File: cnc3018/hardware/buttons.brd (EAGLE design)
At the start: 56 x 20 mm, 4 parts

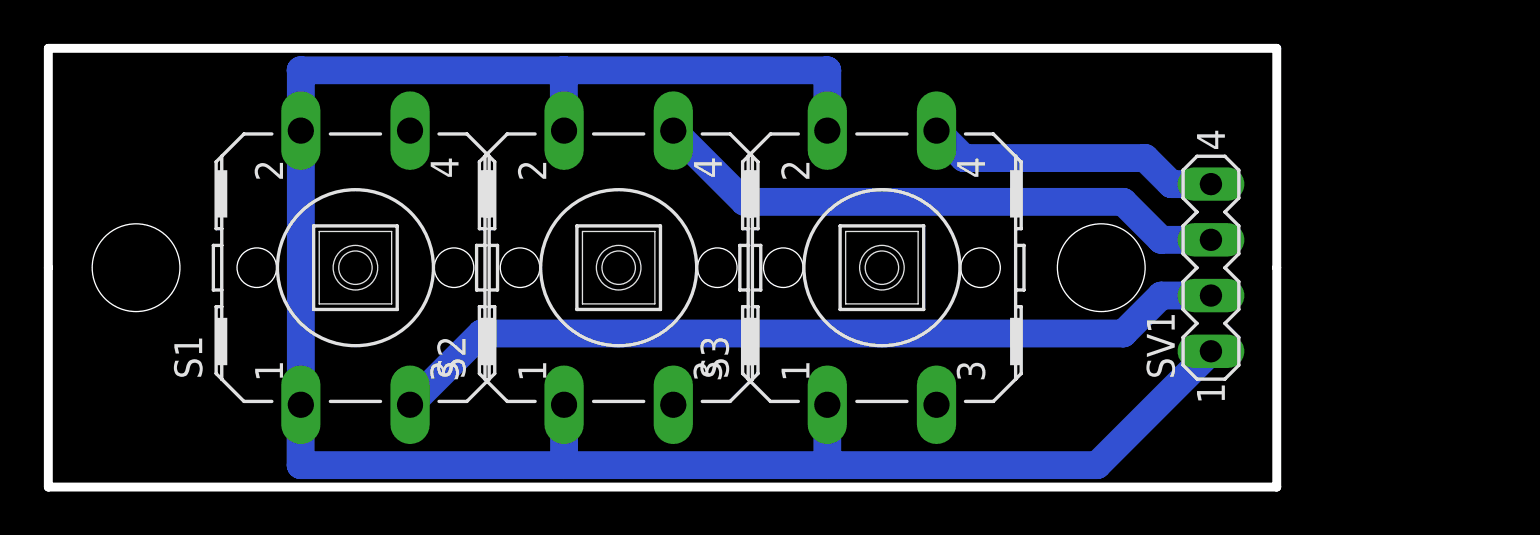
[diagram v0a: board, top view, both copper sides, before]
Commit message: cnc3018: changed buttons board + case
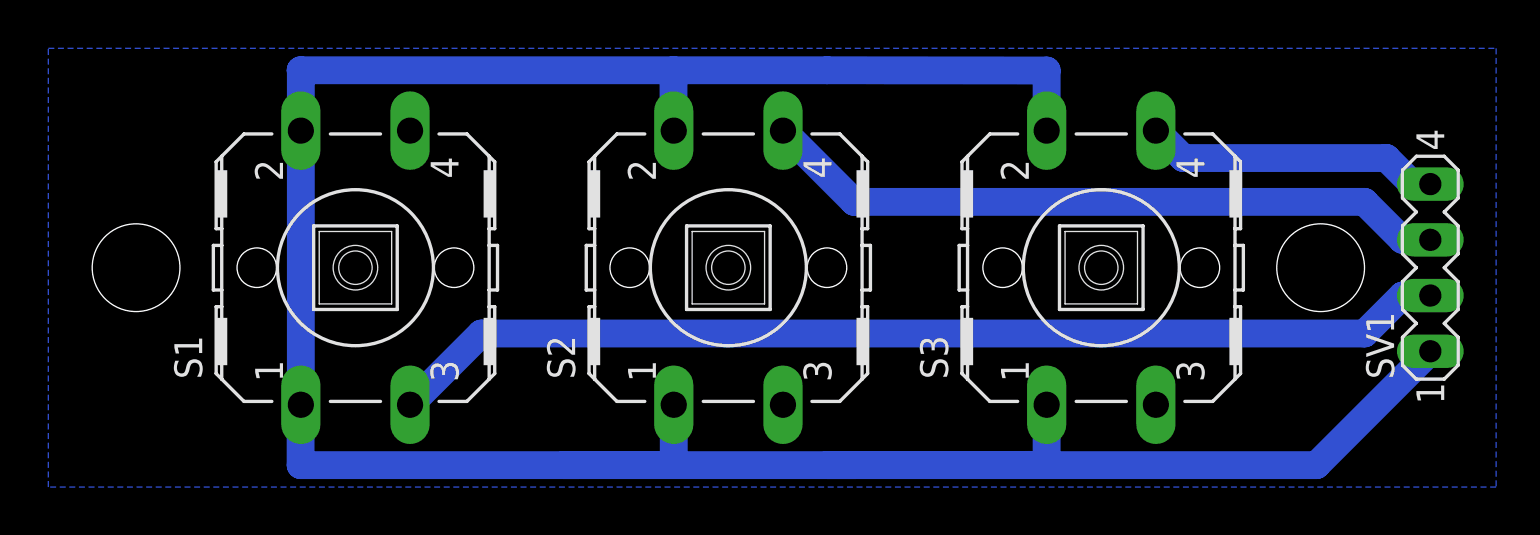
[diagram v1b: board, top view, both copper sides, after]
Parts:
- moved S3 10.0 mm to (48.0, 10.0)
- moved SV1 10.0 mm to (63.0, 10.0)
- moved S2 5.00 mm to (31.0, 10.0)
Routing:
- net GND: track 96.7 -> 131.7 mm
- net N$4: track 38.6 -> 48.6 mm
- net N$3: track 26.6 -> 31.6 mm
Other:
- board outline removed
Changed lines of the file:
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@@
 <board>
 <plain>
-<wire x1="0" y1="0" x2="56" y2="0" width="0.4064" layer="20"/>
-<wire x1="56" y1="0" x2="56" y2="10" width="0.4064" layer="20"/>
-<wire x1="56" y1="10" x2="56" y2="20" width="0.4064" layer="20"/>
-<wire x1="56" y1="20" x2="0" y2="20" width="0.4064" layer="20"/>
-<wire x1="0" y1="20" x2="0" y2="10" width="0.4064" layer="20"/>
-<wire x1="0" y1="10" x2="0" y2="0" width="0.4064" layer="20"/>
 <hole x="4" y="10" drill="4"/>
-<hole x="48" y="10" drill="4"/>
+<hole x="58" y="10" drill="4"/>
 <circle x="4" y="10" radius="3.75" width="0.4064" layer="39"/>
-<circle x="48" y="10" radius="3.75" width="0.4064" layer="39"/>
+<circle x="58" y="10" radius="3.75" width="0.4064" layer="39"/>
 </plain>
 <attributes>
@@
 <attribute name="OC_FARNELL" value="176434" x="14" y="10" size="1.778" layer="27" rot="R90" display="off"/>
 </element>
-<element name="S2" library="switch-omron" package="B3F-40XX" value="" x="26" y="10" rot="R90">
-<attribute name="MPN" value="B3F-4000" x="26" y="10" size="1.778" layer="27" rot="R90" display="off"/>
-<attribute name="OC_NEWARK" value="36K3105" x="26" y="10" size="1.778" layer="27" rot="R90" display="off"/>
-<attribute name="MF" value="OMRON COMPONENTS USA" x="26" y="10" size="1.778" layer="27" rot="R90" display="off"/>
-<attribute name="OC_FARNELL" value="176434" x="26" y="10" size="1.778" layer="27" rot="R90" display="off"/>
-</element>
-<element name="S3" library="switch-omron" package="B3F-40XX" value="" x="38" y="10" rot="R90">
-<attribute name="MPN" value="B3F-4000" x="38" y="10" size="1.778" layer="27" rot="R90" display="off"/>
-<attribute name="OC_NEWARK" value="36K3105" x="38" y="10" size="1.778" layer="27" rot="R90" display="off"/>
-<attribute name="MF" value="OMRON COMPONENTS USA" x="38" y="10" size="1.778" layer="27" rot="R90" display="off"/>
-<attribute name="OC_FARNELL" value="176434" x="38" y="10" size="1.778" layer="27" rot="R90" display="off"/>
-</element>
-<element name="SV1" library="con-lstb" package="MA04-1" value="" x="53" y="10" rot="R90">
-<attribute name="MPN" value="" x="53" y="10" size="1.778" layer="27" rot="R90" display="off"/>
-<attribute name="OC_NEWARK" value="unknown" x="53" y="10" size="1.778" layer="27" rot="R90" display="off"/>
-<attribute name="MF" value="" x="53" y="10" size="1.778" layer="27" rot="R90" display="off"/>
-<attribute name="OC_FARNELL" value="unknown" x="53" y="10" size="1.778" layer="27" rot="R90" display="off"/>
+<element name="S2" library="switch-omron" package="B3F-40XX" value="" x="31" y="10" rot="R90">
+<attribute name="MPN" value="B3F-4000" x="31" y="10" size="1.778" layer="27" rot="R90" display="off"/>
+<attribute name="OC_NEWARK" value="36K3105" x="31" y="10" size="1.778" layer="27" rot="R90" display="off"/>
+<attribute name="MF" value="OMRON COMPONENTS USA" x="31" y="10" size="1.778" layer="27" rot="R90" display="off"/>
+<attribute name="OC_FARNELL" value="176434" x="31" y="10" size="1.778" layer="27" rot="R90" display="off"/>
+</element>
+<element name="S3" library="switch-omron" package="B3F-40XX" value="" x="48" y="10" rot="R90">
+<attribute name="MPN" value="B3F-4000" x="48" y="10" size="1.778" layer="27" rot="R90" display="off"/>
+<attribute name="OC_NEWARK" value="36K3105" x="48" y="10" size="1.778" layer="27" rot="R90" display="off"/>
+<attribute name="MF" value="OMRON COMPONENTS USA" x="48" y="10" size="1.778" layer="27" rot="R90" display="off"/>
+<attribute name="OC_FARNELL" value="176434" x="48" y="10" size="1.778" layer="27" rot="R90" display="off"/>
+</element>
+<element name="SV1" library="con-lstb" package="MA04-1" value="" x="63" y="10" rot="R90">
+<attribute name="MPN" value="" x="63" y="10" size="1.778" layer="27" rot="R90" display="off"/>
+<attribute name="OC_NEWARK" value="unknown" x="63" y="10" size="1.778" layer="27" rot="R90" display="off"/>
+<attribute name="MF" value="" x="63" y="10" size="1.778" layer="27" rot="R90" display="off"/>
+<attribute name="OC_FARNELL" value="unknown" x="63" y="10" size="1.778" layer="27" rot="R90" display="off"/>
 </element>
 </elements>
@@
 <contactref element="S3" pad="4"/>
 <contactref element="SV1" pad="4"/>
-<wire x1="53" y1="13.81" x2="51.19" y2="13.81" width="1.27" layer="16"/>
-<wire x1="51.19" y1="13.81" x2="50" y2="15" width="1.27" layer="16"/>
-<wire x1="50" y1="15" x2="41.7376" y2="15" width="1.27" layer="16"/>
-<wire x1="41.7376" y1="15" x2="40.4892" y2="16.2484" width="1.27" layer="16"/>
+<wire x1="63" y1="13.81" x2="62.19" y2="13.81" width="1.27" layer="16"/>
+<wire x1="62.19" y1="13.81" x2="61" y2="15" width="1.27" layer="16"/>
+<wire x1="61" y1="15" x2="51.7376" y2="15" width="1.27" layer="16"/>
+<wire x1="51.7376" y1="15" x2="50.4892" y2="16.2484" width="1.27" layer="16"/>
 </signal>
 <signal name="N$3">
 <contactref element="SV1" pad="3"/>
 <contactref element="S2" pad="4"/>
-<wire x1="53" y1="11.27" x2="50.73" y2="11.27" width="1.27" layer="16"/>
-<wire x1="50.73" y1="11.27" x2="49" y2="13" width="1.27" layer="16"/>
-<wire x1="49" y1="13" x2="31.7376" y2="13" width="1.27" layer="16"/>
-<wire x1="31.7376" y1="13" x2="28.4892" y2="16.2484" width="1.27" layer="16"/>
+<wire x1="63" y1="11.27" x2="61.73" y2="11.27" width="1.27" layer="16"/>
+<wire x1="61.73" y1="11.27" x2="60" y2="13" width="1.27" layer="16"/>
+<wire x1="60" y1="13" x2="36.7376" y2="13" width="1.27" layer="16"/>
+<wire x1="36.7376" y1="13" x2="33.4892" y2="16.2484" width="1.27" layer="16"/>
 </signal>
 <signal name="N$4">
 <contactref element="SV1" pad="2"/>
 <contactref element="S1" pad="3"/>
-<wire x1="53" y1="8.73" x2="50.73" y2="8.73" width="1.27" layer="16"/>
-<wire x1="50.73" y1="8.73" x2="49" y2="7" width="1.27" layer="16"/>
-<wire x1="49" y1="7" x2="19.7376" y2="7" width="1.27" layer="16"/>
+<wire x1="63" y1="8.73" x2="61.73" y2="8.73" width="1.27" layer="16"/>
+<wire x1="61.73" y1="8.73" x2="60" y2="7" width="1.27" layer="16"/>
+<wire x1="60" y1="7" x2="19.7376" y2="7" width="1.27" layer="16"/>
 <wire x1="19.7376" y1="7" x2="16.4892" y2="3.7516" width="1.27" layer="16"/>
 </signal>
@@
 <vertex x="0" y="0"/>
 <vertex x="0" y="20"/>
-<vertex x="56" y="20"/>
-<vertex x="56" y="0"/>
+<vertex x="66" y="20"/>
+<vertex x="66" y="0"/>
 </polygon>
 <contactref element="S3" pad="2"/>
@@
 <contactref element="S2" pad="2"/>
 <contactref element="S3" pad="1"/>
-<wire x1="35.5" y1="1" x2="47.81" y2="1" width="1.27" layer="16"/>
-<wire x1="47.81" y1="1" x2="53" y2="6.19" width="1.27" layer="16"/>
+<wire x1="35.5" y1="1" x2="57.81" y2="1" width="1.27" layer="16"/>
+<wire x1="57.81" y1="1" x2="63" y2="6.19" width="1.27" layer="16"/>
 <wire x1="11.5108" y1="3.7516" x2="11.5108" y2="16.2484" width="1.27" layer="16"/>
-<wire x1="23.5108" y1="3.7516" x2="23.5108" y2="1.0108" width="1.27" layer="16"/>
-<wire x1="23.5108" y1="1.0108" x2="23.5" y2="1" width="1.27" layer="16"/>
+<wire x1="28.5108" y1="3.7516" x2="28.5108" y2="1.0108" width="1.27" layer="16"/>
+<wire x1="28.5108" y1="1.0108" x2="23.5" y2="1" width="1.27" layer="16"/>
 <wire x1="23.5" y1="1" x2="11.5" y2="1" width="1.27" layer="16"/>
 <wire x1="11.5" y1="1" x2="11.5" y2="3.7408" width="1.27" layer="16"/>
 <wire x1="11.5" y1="3.7408" x2="11.5108" y2="3.7516" width="1.27" layer="16"/>
-<wire x1="35.5108" y1="3.7516" x2="35.5108" y2="1.0108" width="1.27" layer="16"/>
-<wire x1="35.5108" y1="1.0108" x2="35.5" y2="1" width="1.27" layer="16"/>
+<wire x1="45.5108" y1="3.7516" x2="45.5108" y2="1.0108" width="1.27" layer="16"/>
+<wire x1="45.5108" y1="1.0108" x2="35.5" y2="1" width="1.27" layer="16"/>
 <wire x1="35.5" y1="1" x2="23.5" y2="1" width="1.27" layer="16"/>
 <wire x1="11.5108" y1="16.2484" x2="11.5108" y2="18.9892" width="1.27" layer="16"/>
 <wire x1="11.5108" y1="18.9892" x2="11.5" y2="19" width="1.27" layer="16"/>
-<wire x1="11.5" y1="19" x2="23.5" y2="19" width="1.27" layer="16"/>
-<wire x1="23.5" y1="19" x2="23.5" y2="16.2592" width="1.27" layer="16"/>
-<wire x1="23.5" y1="16.2592" x2="23.5108" y2="16.2484" width="1.27" layer="16"/>
-<wire x1="35.5108" y1="16.2484" x2="35.5108" y2="18.9892" width="1.27" layer="16"/>
-<wire x1="35.5108" y1="18.9892" x2="35.5" y2="19" width="1.27" layer="16"/>
-<wire x1="35.5" y1="19" x2="23.5" y2="19" width="1.27" layer="16"/>
+<wire x1="11.5" y1="19" x2="28.5" y2="19" width="1.27" layer="16"/>
+<wire x1="28.5" y1="19" x2="28.5" y2="17.2592" width="1.27" layer="16"/>
+<wire x1="28.5" y1="17.2592" x2="28.5108" y2="16.2484" width="1.27" layer="16"/>
+<wire x1="45.5108" y1="16.2484" x2="45.5108" y2="18.9892" width="1.27" layer="16"/>
+<wire x1="45.5108" y1="18.9892" x2="35.5" y2="19" width="1.27" layer="16"/>
+<wire x1="35.5" y1="19" x2="28.5" y2="19" width="1.27" layer="16"/>
 </signal>
 </signals>
